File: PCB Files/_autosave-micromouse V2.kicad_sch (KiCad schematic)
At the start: 59 parts, among them J1 TOF1, J2 TOF1, J3 Conn_02x02_Counter_Clockwise, J4 BATT, J5 TOF1, J6 Conn_01x02_Pin, J7 Motor 1, J8 Motor 2, J9 USB-C, SW1 BOOT0, SW2 BOOT1, SW3 A, SW4 B, SW5 C, SW6 RESET, SW7 POWER, U1 L7806, U2 AMS1117-3.3, U3 L7805, U4 STM32F103C8Tx, U5 SSD1306, U6 TB6612FNG, X1 SG-3030CM, Y1 8MHz, Y2 32.768K

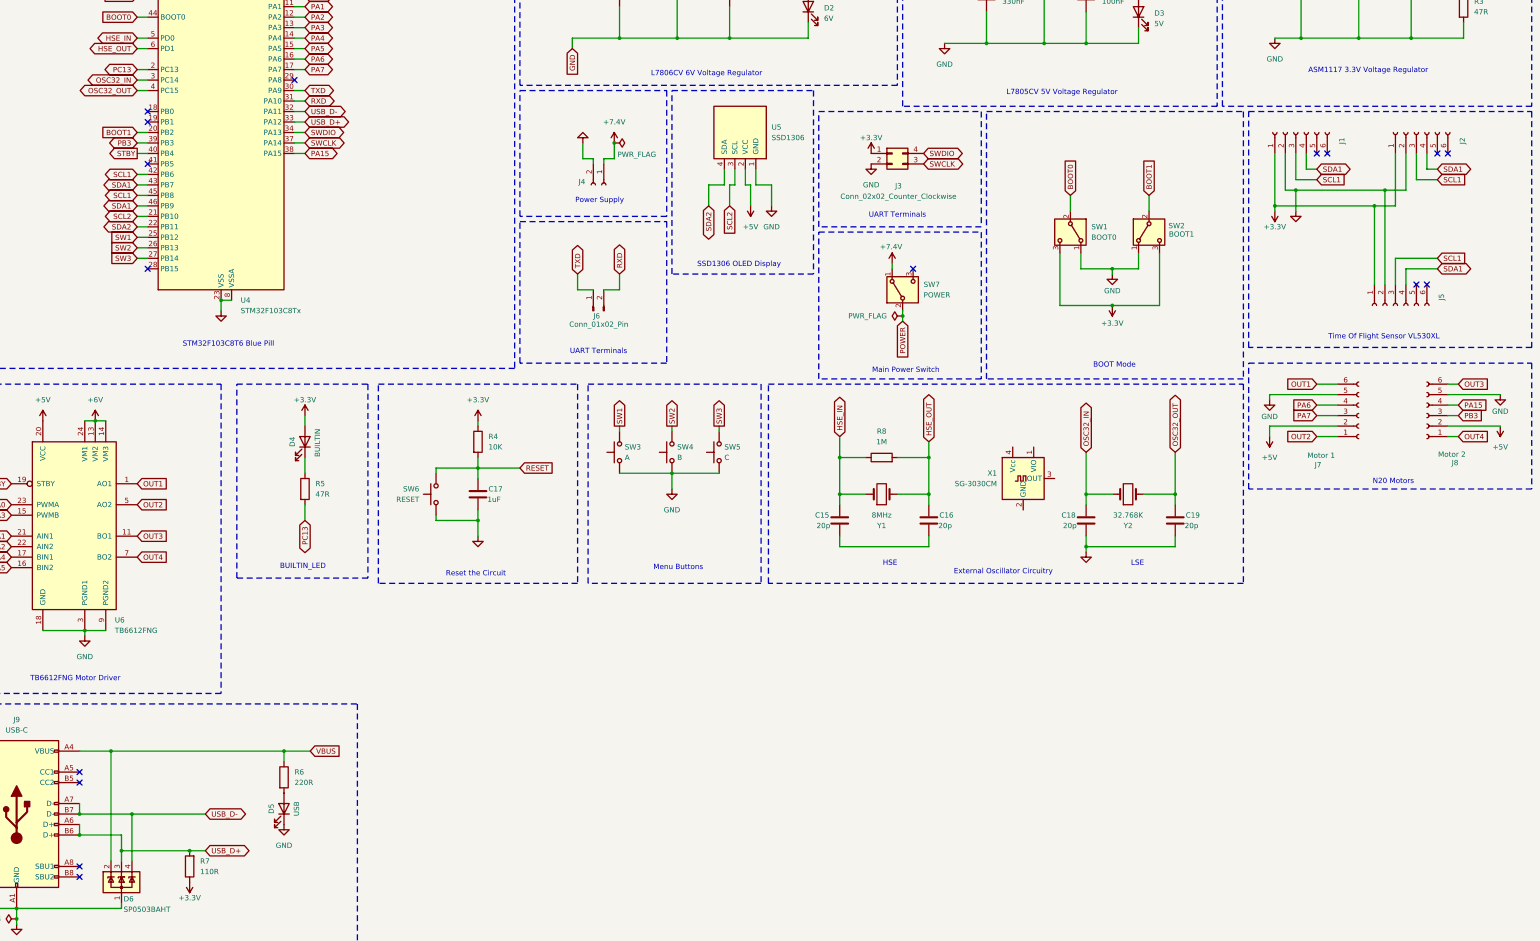
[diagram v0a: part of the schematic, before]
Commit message: Assigned HSE and LSE Oscillators
HSE - ABLS2-8.000MHZ-D4Y-T
LSE - ABS07-32.768KHZ-T
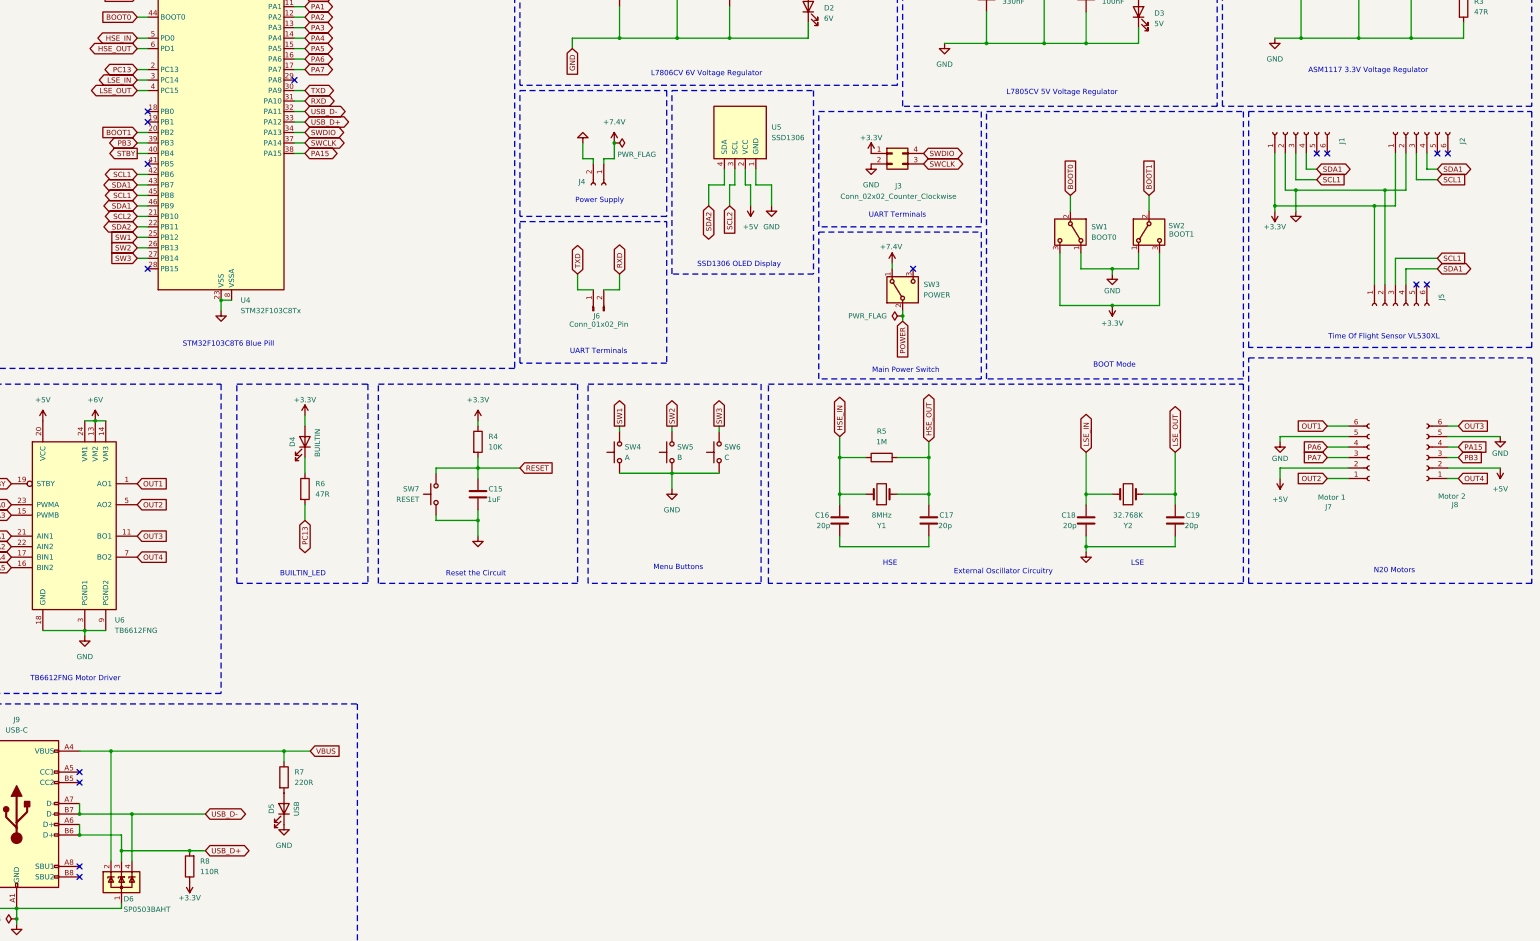
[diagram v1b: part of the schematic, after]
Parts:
- removed X1: SG-3030CM, Oscillator:Oscillator_SMD_SeikoEpson_SG3030CM, symbol Oscillator:SG-3030CM
- Y1: footprint Crystal:Crystal_HC49-4H_Vertical -> Custom:Crystal_ABLS2-8.000MHZ-D4Y-T
- Y2: footprint Custom:Crystal_ABLS2-8.000MHZ-D4Y-T -> Custom:XTAL_ABS07-32.768KHZ-T
- renumbered C17 to C15, C15 to C16, C16 to C17, R8 to R5, R5 to R6, R6 to R7, R7 to R8, SW7 to SW3, SW3 to SW4, SW4 to SW5, SW5 to SW6, SW6 to SW7
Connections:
- net OSC32_IN renamed LSE_IN
- net OSC32_OUT renamed LSE_OUT
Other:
- moved on the sheet: J7, J8
